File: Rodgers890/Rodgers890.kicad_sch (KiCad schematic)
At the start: 72 parts, among them J1 Conn_01x30_Pin, J2 Conn_01x02_Pin, Q1 BC817, Q2 BC807, Q3 BC817, Q4 BC807, U1 7417, U2 4050

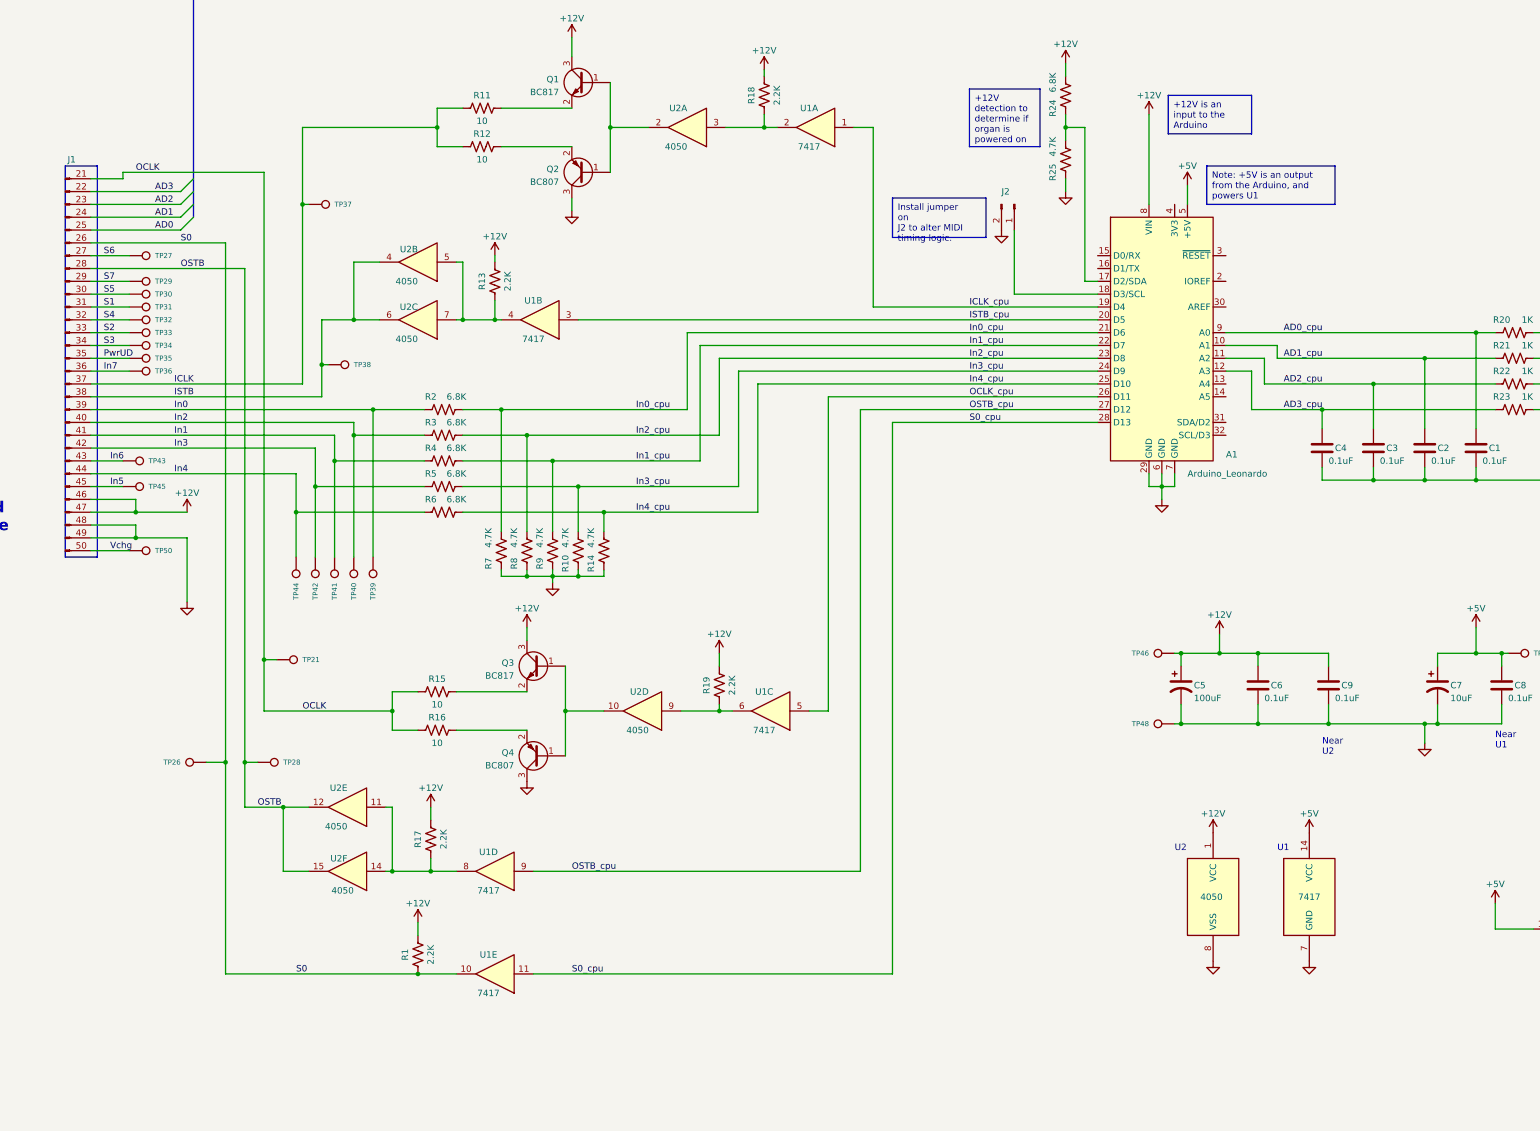
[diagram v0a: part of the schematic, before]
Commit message: Address Issue #4: Wrong output chain used, for schematic only. Revision marking on schematic becomes “Rev 0.2”
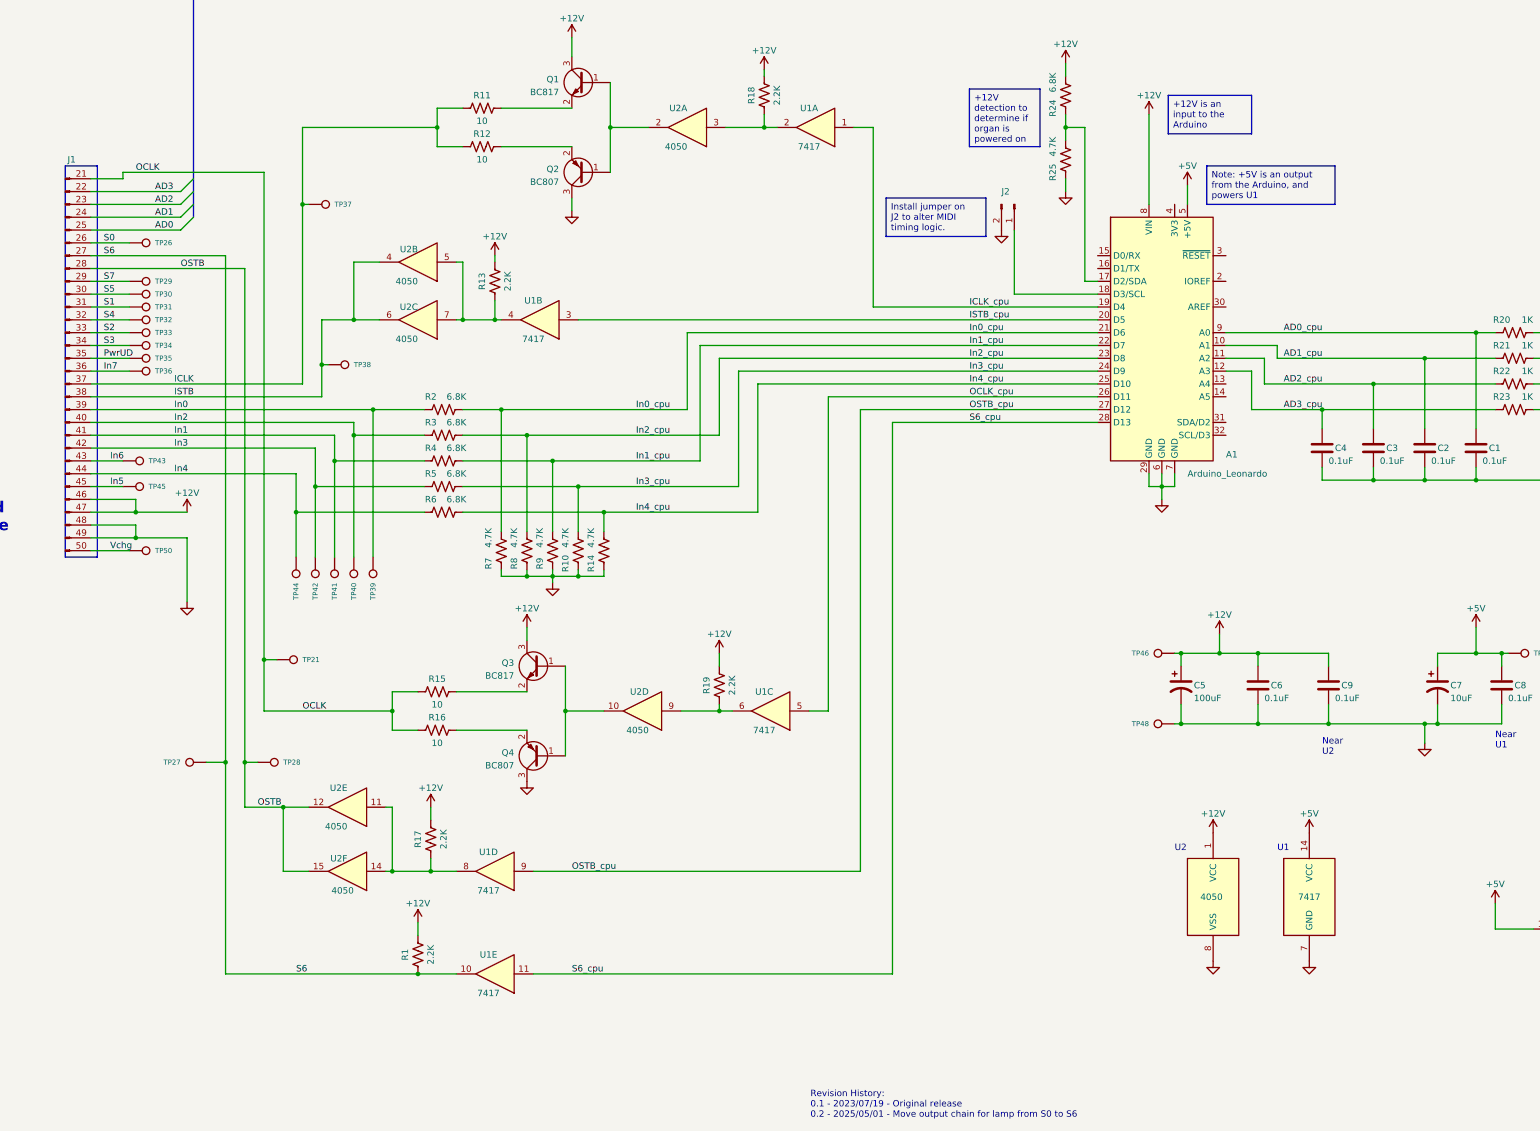
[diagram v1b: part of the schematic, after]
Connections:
- net S0: no longer R1.1, U1.10
- net S6: now also R1.1, U1.10
- net S0_cpu renamed S6_cpu
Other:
- note added: "Revision History: 0.1 - 2023/07/19 - Original release 0.2 - 2025/05/01 - Move output chain for lamp from S0 to S6"
- moved on the sheet: TP26, TP27

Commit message: Ready for first schematic review with James
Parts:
- removed A1: Arduino_Leonardo, Module:Arduino_UNO_R3, symbol MCU_Module:Arduino_Leonardo
- added C10: 0.1uF, Capacitor_SMD:C_0603_1608Metric_Pad1.08x0.95mm_HandSolder, symbol Device:C
- added D1: 1N914, Diode_THT:D_DO-35_SOD27_P7.62mm_Horizontal, symbol Diode:1N914
- added J4, J5: DIN-5_180degree, symbol Connector:DIN-5_180degree
- added R26, R27, R28, R29, R30, R31: 3.0K, Resistor_SMD:R_0603_1608Metric_Pad0.98x0.95mm_HandSolder, symbol Device:R_US
- added R32: 220, Resistor_SMD:R_0603_1608Metric_Pad0.98x0.95mm_HandSolder, symbol Device:R_US
- added R33: 470, Resistor_SMD:R_0603_1608Metric_Pad0.98x0.95mm_HandSolder, symbol Device:R_US
- added R34: 33, Resistor_SMD:R_0603_1608Metric_Pad0.98x0.95mm_HandSolder, symbol Device:R_US
- added R35: 10, Resistor_SMD:R_0603_1608Metric_Pad0.98x0.95mm_HandSolder, symbol Device:R_US
- added R36, R38, R40, R42: 180K, Resistor_SMD:R_0603_1608Metric_Pad0.98x0.95mm_HandSolder, symbol Device:R_US
- added R37, R39, R41, R43: 300K, Resistor_SMD:R_0603_1608Metric_Pad0.98x0.95mm_HandSolder, symbol Device:R_US
- added U3: ESP32-S3-DevKitM-1, PCM_Espressif:ESP32-S3-DevKitM, symbol MCU_Module:ESP32-S3-DevKitM-1
- added U4: LM78M05_TO252, Package_TO_SOT_SMD:TO-252-2, symbol Regulator_Linear:LM78M05_TO252
- added U5: Arduino_Pro_Micro, Rogers890Library:Arduino_Pro_Micro, symbol MCU_Module:Arduino_Pro_Micro
- added U7: H11L1, symbol Isolator:H11L1
- R10, R14, R25, R7, R8, R9: value 4.7K -> 1.8K
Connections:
- net +12V: now also U4.1 (VI), U5.24 (RAW)
- net +5V: now also C10.1, U3.21 (5V0), U4.3 (VO)
- net AD0_cpu: now also R36.1, U5.17 (A0)
- net AD1_cpu: now also R38.1, U5.18 (A1)
- net AD2_cpu: now also R40.1, U5.19 (A2)
- net AD3_cpu: now also R42.1, U5.20 (A3)
- net GND: now also C10.2, J5.2, R26.1, R27.1, R28.1, R29.1, R30.1, R31.1, R37.2, R39.2, R41.2, R43.2, U3.22 (GND), U3.44 (GND), U4.2 (GND), U5.23 (GND), U5.3 (GND), U5.4 (GND), U7.5; no longer R10.1, R14.1, R25.1, R7.1, R8.1, R9.1
- net ICLK_cpu: now also U3.7 (GPIO5), U5.7 (D4)
- net ISTB_cpu: now also U3.8 (GPIO6), U5.8 (D5)
- net OCLK_cpu: now also U3.14 (GPIO12), U5.15 (D14)
- net OSTB_cpu: now also U3.15 (GPIO13), U5.16 (D15)
- net S6_cpu: now also U3.16 (GPIO14), U5.14 (D16)
- net at R24.1, R25.2: now also U5.5 (D2)
- net at J2.1 (Pin_1): now also U3.17 (GPIO15), U5.6 (D3)
- net In0_cpu renamed In0_ard
- net In0_ard: now also U5.9 (D6)
- net In1_cpu renamed In1_ard
- net In1_ard: now also U5.10 (D7)
- net In2_cpu renamed In2_ard
- net In2_ard: now also U5.11 (D8)
- net In3_cpu renamed In3_ard
- net In3_ard: now also U5.12 (D9)
- net In4_cpu renamed In4_ard
- net In4_ard: now also U5.13 (D10)
- new net: R25.1, R31.2, U3.18 (GPIO16)
- new net: R40.2, R41.1, U3.5 (GPIO3)
- new net: J4.4, R32.1
- new net: D1.1 (K), R32.2, U7.1
- new net: J5.5, R35.1
- new net: R35.2, U3.19 (GPIO17)
- new net: R36.2, R37.1, U3.3 (GPIO1)
- new net: D1.2 (A), J4.5, U7.2
- new net: R38.2, R39.1, U3.4 (GPIO2)
- new net: R33.1, U3.20 (GPIO18), U7.4
- new net: R42.2, R43.1, U3.6 (GPIO4)
- new net: J5.4, R34.1
- new net +3V3: R33.2, R34.2, U3.1 (3V3), U7.6
- new net In0_esp: R30.2, R7.1, U3.9 (GPIO7)
- new net In1_esp: R27.2, R9.1, U3.10 (GPIO8)
- new net In2_esp: R26.2, R8.1, U3.11 (GPIO9)
- new net In3_esp: R10.1, R28.2, U3.12 (GPIO10)
- new net In4_esp: R14.1, R29.2, U3.13 (GPIO11)
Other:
- note added: "Install one of these, but not both."
- note added: "MIDI In"
- note added: "MIDI Out"
- note added: "Near U3"
- note added: "Provides +5V for U1 and U3 (if installed)"
- note added: "Revision History: 0.1 - 2023/07/19 - Original release 0.2 - 2025/05/01 - Move output chain for lamp from S0 to S6 0.3 - 2025/05/07 - CPU is either Arduino Pro Micro, or ESP32"
- note removed: "Revision History: 0.1 - 2023/07/19 - Original release 0.2 - 2025/05/01 - Move output chain for lamp from S0 to S6"
- moved on the sheet: C5, C6, C7, C8, C9, J2, Q3, Q4, R1, R10, R14, R15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
